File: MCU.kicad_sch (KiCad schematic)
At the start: 26 parts, among them J1 FTSH-105-01-L-DV-K-A, J2 USB_C_Receptacle_USB2.0_16P, U1 STM32G0B1CBTx, Y1 Crystal_GND24, Y2 32.768 kHz 6pF

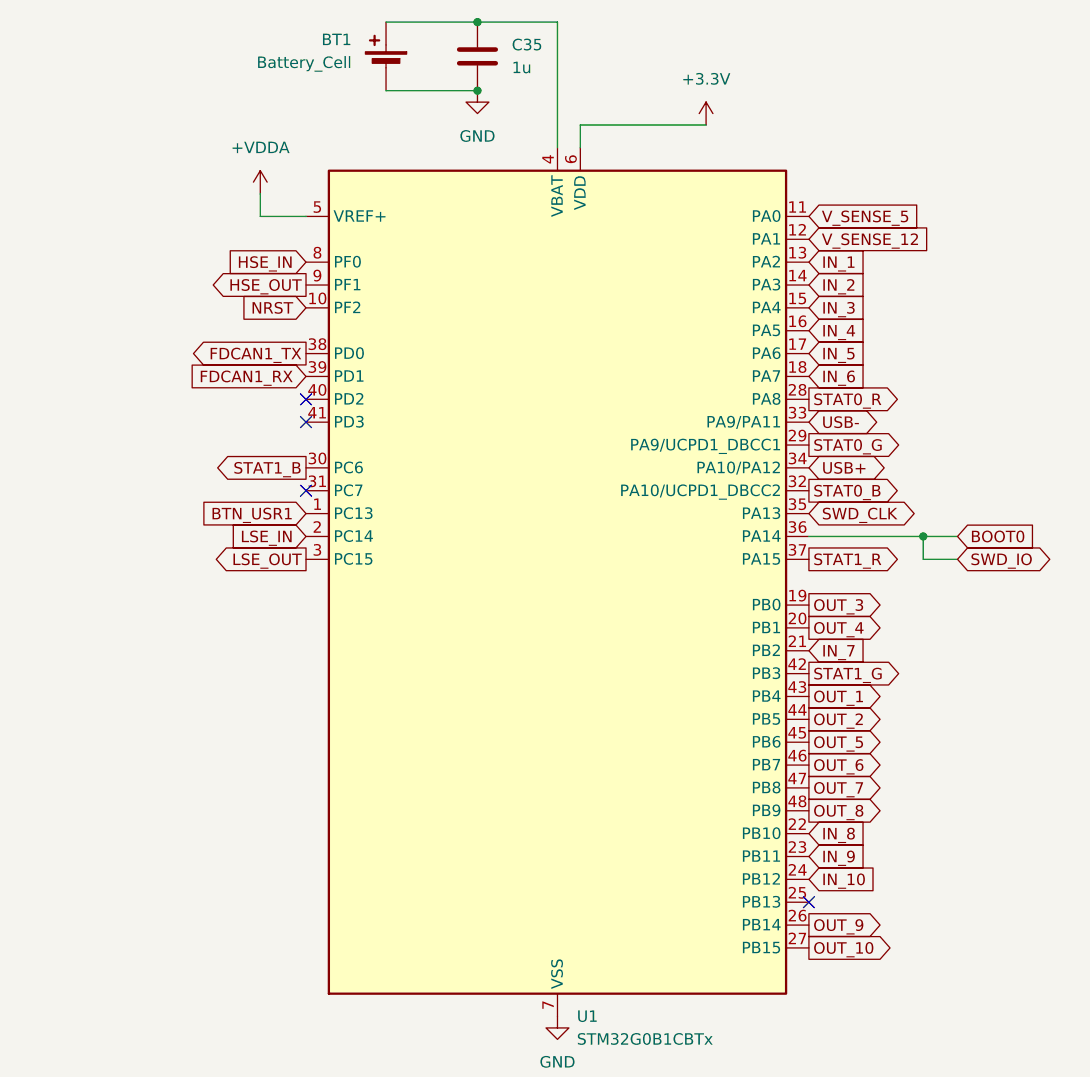
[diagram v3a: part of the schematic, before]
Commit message: dual H/V compatible Molex footprints, corrected STM32 pinout
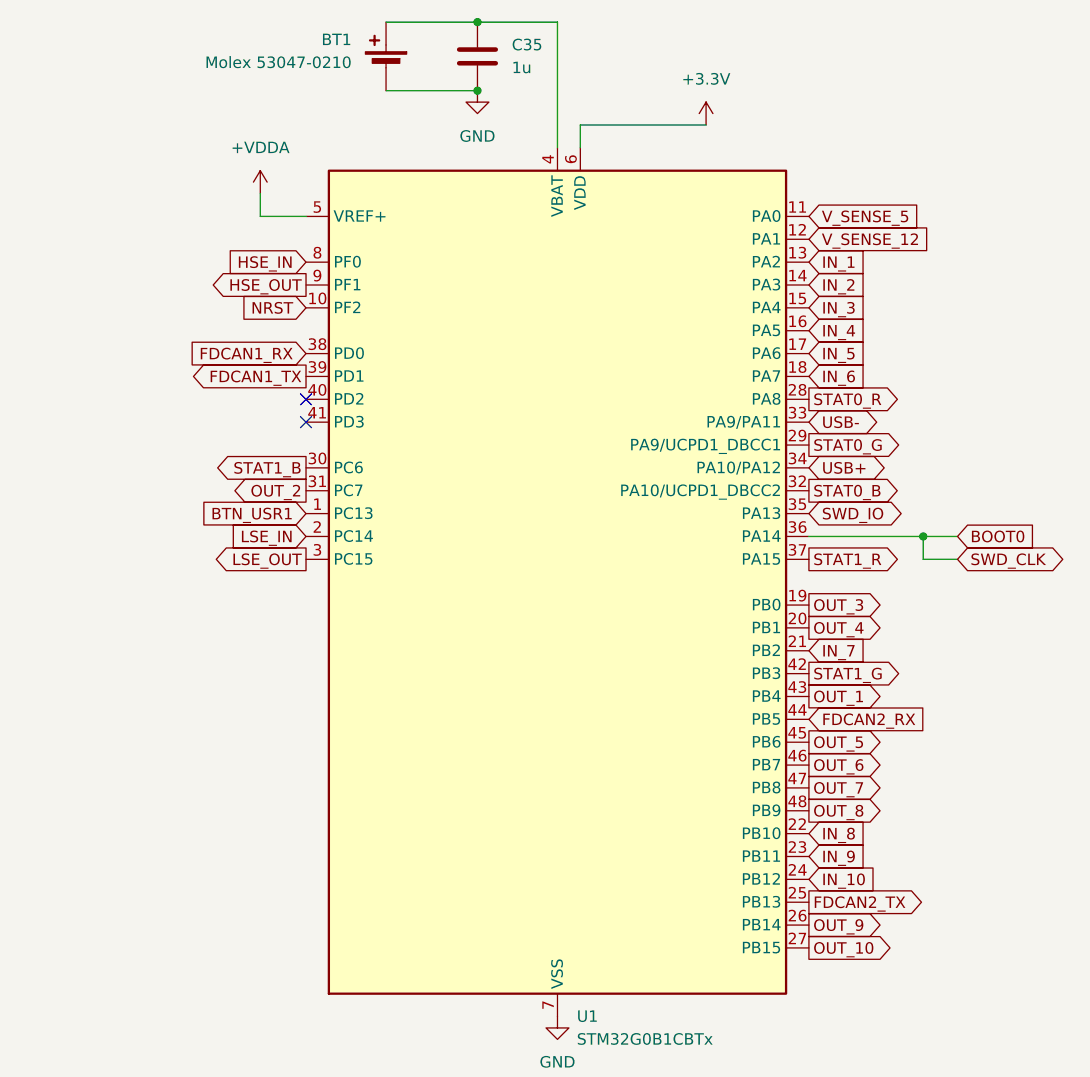
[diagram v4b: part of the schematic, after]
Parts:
- BT1: value Battery_Cell -> Molex 53047-0210; footprint (none) -> Connector_Molex:Molex_PicoBlade_53047-0210_1x02_P1.25mm_Vertical
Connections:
- net BOOT0: now also J1.4; no longer J1.2
- net FDCAN1_RX: now also U1.38 (PD0); no longer U1.39 (PD1)
- net FDCAN1_TX: now also U1.39 (PD1); no longer U1.38 (PD0)
- net OUT_2: now also U1.31 (PC7); no longer U1.44 (PB5)
- net FDCAN2_TX: now reaches U1.25 (PB13)
- net SWD_CLK renamed SWD_IO
- net SWD_IO: now also J1.2; no longer J1.4
- new net FDCAN2_RX: U1.44 (PB5)
- no-connect marks 9 -> 7
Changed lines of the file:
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@@
 	)
 	(no_connect
-		(at 195.58 69.85)
-	)
-	(no_connect
 		(at 73.66 142.24)
 	)
@@
 	)
 	(no_connect
-		(at 251.46 115.57)
-	)
-	(no_connect
 		(at 195.58 59.69)
 	)
@@
 		)
 	)
-	(global_label "SWD_CLK"
+	(global_label "SWD_IO"
 		(shape bidirectional)
 		(at 251.46 72.39 0)
@@
 		)
 		(property "Intersheetrefs" "${INTERSHEET_REFS}"
-			(at 264.0231 72.39 0)
+			(at 262.3903 72.39 0)
 			(hide yes)
 			(show_name no)
@@
 		)
 	)
+	(global_label "FDCAN2_TX"
+		(shape output)
+		(at 251.46 115.57 0)
+		(fields_autoplaced yes)
+		(effects
+			(font
+				(size 1.27 1.27)
+			)
+			(justify left)
+		)
+		(property "Intersheetrefs" "${INTERSHEET_REFS}"
+			(at 264.8471 115.57 0)
+			(hide yes)
+			(show_name no)
+			(do_not_autoplace no)
+			(effects
+				(font
+					(size 1.27 1.27)
+				)
+				(justify left)
+			)
+		)
+	)
 	(global_label "STAT1_G"
 		(shape input)
@@
 	(global_label "FDCAN1_RX"
 		(shape input)
-		(at 195.58 57.15 180)
+		(at 195.58 54.61 180)
 		(fields_autoplaced yes)
 		(effects
@@
 		)
 		(property "Intersheetrefs" "${INTERSHEET_REFS}"
-			(at 181.8905 57.15 0)
+			(at 181.8905 54.61 0)
 			(hide yes)
 			(show_name no)
@@
 	(global_label "OUT_2"
 		(shape output)
-		(at 251.46 95.25 0)
+		(at 195.58 69.85 180)
 		(fields_autoplaced yes)
 		(effects
@@
 				(size 1.27 1.27)
 			)
-			(justify left)
+			(justify right)
 		)
 		(property "Intersheetrefs" "${INTERSHEET_REFS}"
-			(at 260.2509 95.25 0)
+			(at 186.7891 69.85 0)
 			(hide yes)
 			(show_name no)
@@
 					(size 1.27 1.27)
 				)
-				(justify left)
+				(justify right)
 			)
 		)
@@
 		)
 	)
+	(global_label "FDCAN2_RX"
+		(shape input)
+		(at 251.46 95.25 0)
+		(fields_autoplaced yes)
+		(effects
+			(font
+				(size 1.27 1.27)
+			)
+			(justify left)
+		)
+		(property "Intersheetrefs" "${INTERSHEET_REFS}"
+			(at 265.1495 95.25 0)
+			(hide yes)
+			(show_name no)
+			(do_not_autoplace no)
+			(effects
+				(font
+					(size 1.27 1.27)
+				)
+				(justify left)
+			)
+		)
+	)
 	(global_label "STAT1_B"
 		(shape input)
@@
 		)
 	)
-	(global_label "SWD_IO"
+	(global_label "SWD_CLK"
 		(shape bidirectional)
 		(at 267.97 77.47 0)
@@
 		)
 		(property "Intersheetrefs" "${INTERSHEET_REFS}"
-			(at 278.9003 77.47 0)
+			(at 280.5331 77.47 0)
 			(hide yes)
 			(show_name no)
@@
 	(global_label "FDCAN1_TX"
 		(shape output)
-		(at 195.58 54.61 180)
+		(at 195.58 57.15 180)
 		(fields_autoplaced yes)
 		(effects
@@
 		)
 		(property "Intersheetrefs" "${INTERSHEET_REFS}"
-			(at 182.1929 54.61 0)
+			(at 182.1929 57.15 0)
 			(hide yes)
 			(show_name no)
@@
 			)
 		)
-		(property "Value" "Battery_Cell"
+		(property "Value" "Molex 53047-0210"
 			(at 200.66 22.2884 0)
 			(show_name no)
@@
 			)
 		)
-		(property "Footprint" ""
+		(property "Footprint" "Connector_Molex:Molex_PicoBlade_53047-0210_1x02_P1.25mm_Vertical"
 			(at 204.47 21.336 90)
 			(hide yes)

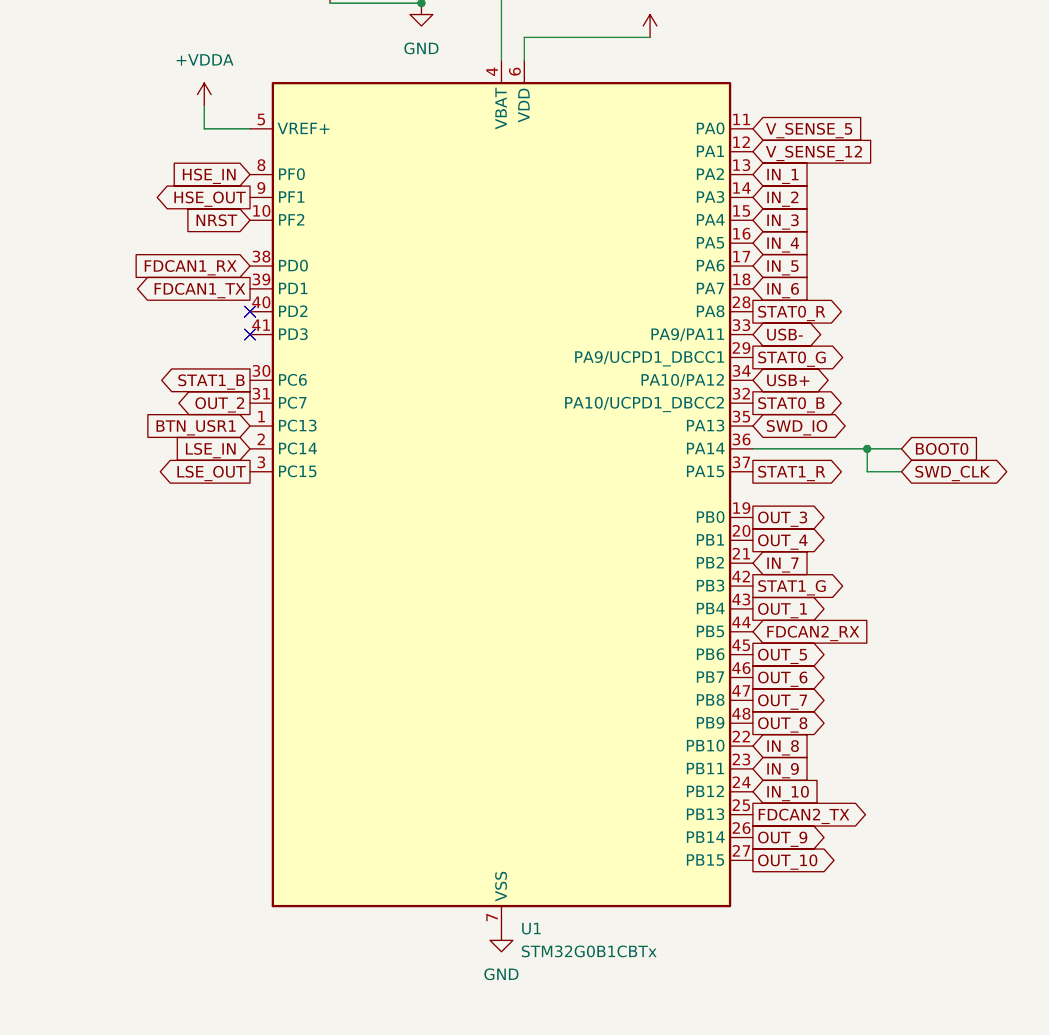
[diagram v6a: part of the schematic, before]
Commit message: full layout routing and silkscreen
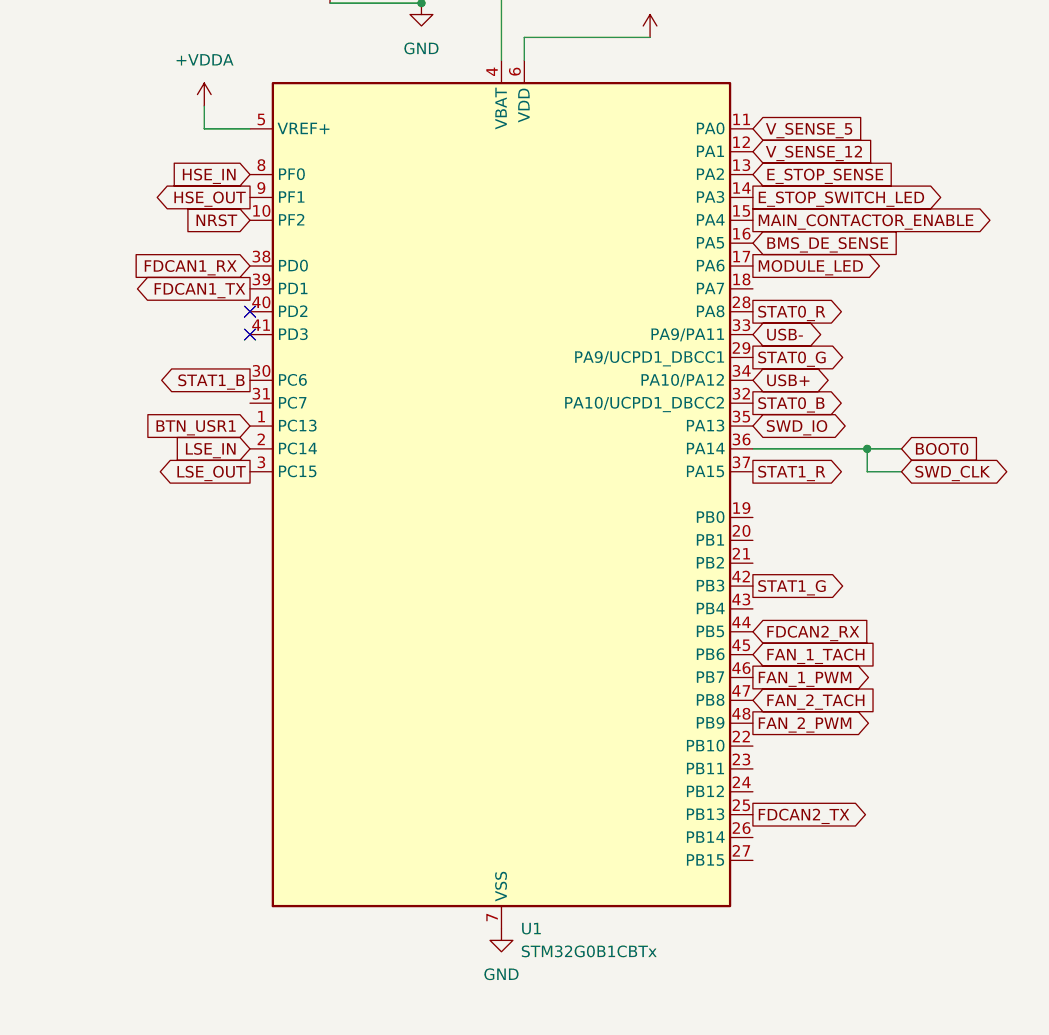
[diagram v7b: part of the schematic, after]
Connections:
- net IN_1 renamed E_STOP_SENSE
- net IN_10: no longer names the net of U1.24 (PB12)
- net IN_2 renamed E_STOP_SWITCH_LED
- net IN_3 renamed MAIN_CONTACTOR_ENABLE
- net IN_4 renamed BMS_DE_SENSE
- net IN_5 renamed MODULE_LED
- net IN_6: no longer names the net of U1.18 (PA7)
- net IN_7: no longer names the net of U1.21 (PB2)
- net IN_8: no longer names the net of U1.22 (PB10)
- net IN_9: no longer names the net of U1.23 (PB11)
- net OUT_1: no longer names the net of U1.43 (PB4)
- net OUT_10: no longer names the net of U1.27 (PB15)
- net OUT_2: no longer names the net of U1.31 (PC7)
- net OUT_3: no longer names the net of U1.19 (PB0)
- net OUT_4: no longer names the net of U1.20 (PB1)
- net OUT_5 renamed FAN_1_TACH
- net OUT_6 renamed FAN_1_PWM
- net OUT_7 renamed FAN_2_TACH
- net OUT_8 renamed FAN_2_PWM
- net OUT_9: no longer names the net of U1.26 (PB14)

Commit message: r0 final
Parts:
- renumbered C35 to C10, C6 to C11, C7 to C12, C1 to C3, C2 to C4, C3 to C5, C8 to C6, C4 to C7, C31 to C8, C5 to C9, D1 to D5, J1 to J8, J2 to J9, R1 to R11, R2 to R12, R3 to R13, R4 to R14, R5 to R15
